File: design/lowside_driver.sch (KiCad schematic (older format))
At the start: 4 parts

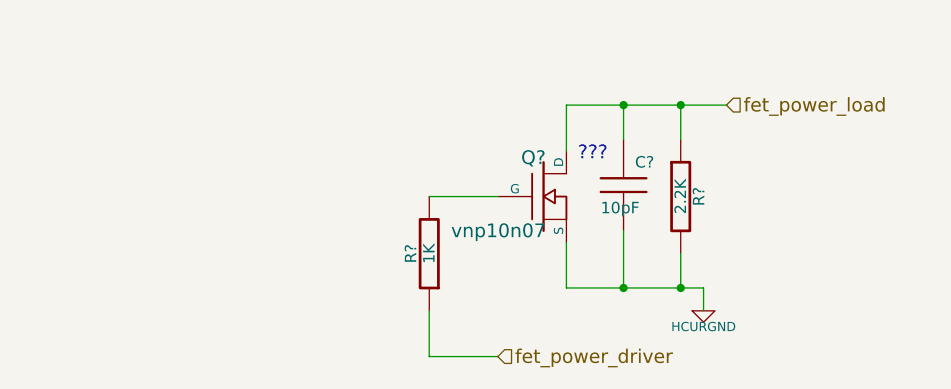
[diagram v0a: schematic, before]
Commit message: Dan's style schema in KiCAD first uploaded
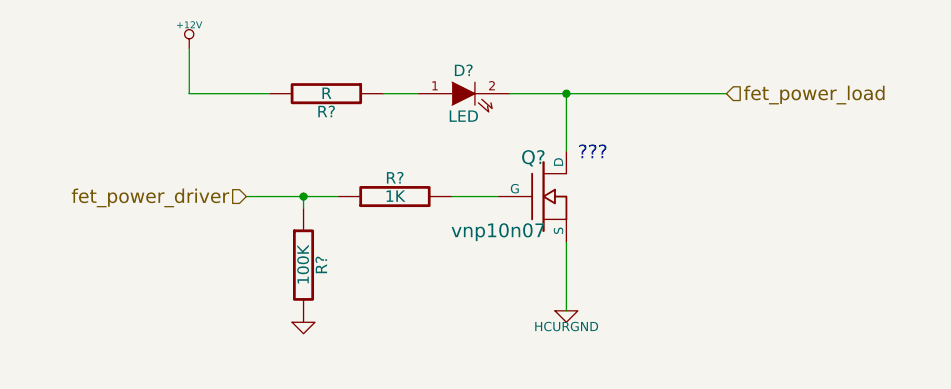
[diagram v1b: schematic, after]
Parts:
- removed C?: 10pF, symbol C
- removed R?: 2.2K, symbol R
- added D?: LED, symbol LED
- added R?: 100K, symbol R
- added R?: R, symbol R
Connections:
- net fet_power_driver: now also R?.1
- net fet_power_load: now also D?.2 (K)
- new net: D?.1 (A), R?.1
- new net +12V: R?.2
- new net GND: R?.2
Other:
- moved on the sheet: R?
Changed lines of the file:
@@
-EESchema Schematic File Version 2  date 08/10/2011 12:36:15
+EESchema Schematic File Version 2  date 10/10/2011 12:34:13
 LIBS:power
 LIBS:device
@@
 EELAYER END
 $Descr A4 11700 8267
-Sheet 14 29
+Sheet 14 20
 Title "low side driver"
-Date "8 oct 2011"
+Date "10 oct 2011"
 Rev "0.01"
 Comp "diyefi.org"
@@
 Comment4 ""
 $EndDescr
-Connection ~ 6150 4150
+Connection ~ 5650 3300
 Wire Wire Line
-	6250 4150 6250 4250
+	5650 3550 5650 3300
 Wire Wire Line
-	6250 4150 5650 4150
-Connection ~ 6150 3350
+	4850 3300 5000 3300
+Connection ~ 4500 3750
 Wire Wire Line
-	6150 3350 6150 3500
+	4500 3800 4500 3750
 Wire Wire Line
-	5900 3900 5900 4150
+	5150 3750 5350 3750
 Wire Wire Line
-	5050 3750 5350 3750
+	4650 3750 4250 3750
 Wire Wire Line
-	5650 3550 5650 3350
+	5650 4250 5650 3950
 Wire Wire Line
-	5900 3500 5900 3350
+	5400 3300 6350 3300
 Wire Wire Line
-	5650 4150 5650 3950
+	4350 3300 4000 3300
 Wire Wire Line
-	5650 3350 6350 3350
-Connection ~ 5900 3350
-Wire Wire Line
-	5050 4250 5050 4450
-Wire Wire Line
-	5050 4450 5350 4450
-Wire Wire Line
-	6150 4150 6150 4000
-Connection ~ 5900 4150
+	4000 3300 4000 3100
+$Comp
+L +12V #PWR?
+U 1 1 4E912486
+P 4000 3100
+AR Path="/4E8D66C5/4E912486" Ref="#PWR?"  Part="1"
+AR Path="/4E8D6593/4E912486" Ref="#PWR?"  Part="1"
+AR Path="/4E8D6540/4E912486" Ref="#PWR?"  Part="1"
+AR Path="/4E8D640E/4E912486" Ref="#PWR?"  Part="1"
+AR Path="/4E8D5F70/4E912486" Ref="#PWR?"  Part="1"
+F 0 "#PWR?" H 4000 3050 20  0001 C CNN
+F 1 "+12V" H 4000 3200 30  0000 C CNN
+	1    4000 3100
+	1    0    0    -1
+$EndComp
 $Comp
 L R R?
-U 1 1 4E8DCA58
-P 6150 3750
-AR Path="/4E8D5F70/4E8DCA58" Ref="R?"  Part="1"
-AR Path="/4E8D6593/4E8DCA58" Ref="R?"  Part="1"
-AR Path="/4E8D64D8/4E8DCA58" Ref="R?"  Part="1"
-AR Path="/4E8D66C5/4E8DCA58" Ref="R?"  Part="1"
-AR Path="/4E8D640E/4E8DCA58" Ref="R?"  Part="1"
-AR Path="/4E8D6540/4E8DCA58" Ref="R?"  Part="1"
-F 0 "R?" V 6230 3750 50  0000 C CNN
-F 1 "2.2K" V 6150 3750 50  0000 C CNN
-	1    6150 3750
+U 1 1 4E912449
+P 4600 3300
+AR Path="/4E8D66C5/4E912449" Ref="R?"  Part="1"
+AR Path="/4E8D6593/4E912449" Ref="R?"  Part="1"
+AR Path="/4E8D6540/4E912449" Ref="R?"  Part="1"
+AR Path="/4E8D640E/4E912449" Ref="R?"  Part="1"
+AR Path="/4E8D5F70/4E912449" Ref="R?"  Part="1"
+F 0 "R?" V 4680 3300 50  0000 C CNN
+F 1 "R" V 4600 3300 50  0000 C CNN
+	1    4600 3300
+	0    1    1    0
+$EndComp
+$Comp
+L LED D?
+U 1 1 4E912443
+P 5200 3300
+AR Path="/4E8D66C5/4E912443" Ref="D?"  Part="1"
+AR Path="/4E8D6593/4E912443" Ref="D?"  Part="1"
+AR Path="/4E8D6540/4E912443" Ref="D?"  Part="1"
+AR Path="/4E8D640E/4E912443" Ref="D?"  Part="1"
+AR Path="/4E8D5F70/4E912443" Ref="D?"  Part="1"
+F 0 "D?" H 5200 3400 50  0000 C CNN
+F 1 "LED" H 5200 3200 50  0000 C CNN
+	1    5200 3300
+	1    0    0    -1
+$EndComp
+$Comp
+L GND #PWR?
+U 1 1 4E91226E
+P 4500 4300
+AR Path="/4E8D6593/4E91226E" Ref="#PWR?"  Part="1"
+AR Path="/4E8D6540/4E91226E" Ref="#PWR?"  Part="1"
+AR Path="/4E8D66C5/4E91226E" Ref="#PWR?"  Part="1"
+AR Path="/4E8D640E/4E91226E" Ref="#PWR?"  Part="1"
+AR Path="/4E8D5F70/4E91226E" Ref="#PWR?"  Part="1"
+F 0 "#PWR?" H 4500 4300 30  0001 C CNN
+F 1 "GND" H 4500 4230 30  0001 C CNN
+	1    4500 4300
+	1    0    0    -1
+$EndComp
+$Comp
+L R R?
+U 1 1 4E91207E
+P 4500 4050
+AR Path="/4E8D6593/4E91207E" Ref="R?"  Part="1"
+AR Path="/4E8D6540/4E91207E" Ref="R?"  Part="1"
+AR Path="/4E8D66C5/4E91207E" Ref="R?"  Part="1"
+AR Path="/4E8D640E/4E91207E" Ref="R?"  Part="1"
+AR Path="/4E8D5F70/4E91207E" Ref="R?"  Part="1"
+F 0 "R?" V 4580 4050 50  0000 C CNN
+F 1 "100K" V 4500 4050 50  0000 C CNN
+	1    4500 4050
 	1    0    0    -1
 $EndComp
@@
 L HCURGND #PWR?
 U 1 1 4E8D6378
-P 6250 4250
+P 5650 4250
 AR Path="/4E8D5F70/4E8D6378" Ref="#PWR?"  Part="1"
 AR Path="/4E8D640E/4E8D6378" Ref="#PWR?"  Part="1"
@@
 AR Path="/4E8D6593/4E8D6378" Ref="#PWR?"  Part="1"
 AR Path="/4E8D6540/4E8D6378" Ref="#PWR?"  Part="1"
-F 0 "#PWR?" H 6250 4250 40  0001 C CNN
-F 1 "HCURGND" H 6250 4180 40  0000 C CNN
-	1    6250 4250
+F 0 "#PWR?" H 5650 4250 40  0001 C CNN
+F 1 "HCURGND" H 5650 4180 40  0000 C CNN
+	1    5650 4250
 	1    0    0    -1
 $EndComp
-Text HLabel 6350 3350 2    60   Input ~ 0
+Text HLabel 6350 3300 2    60   Input ~ 0
 fet_power_load
 Text Notes 5700 3600 0    60   ~ 0
 ???
-$Comp
-L C C?
-U 1 1 4E8D61E7
-P 5900 3700
-AR Path="/4E8D5F70/4E8D61E7" Ref="C?"  Part="1"
-AR Path="/4E8D640E/4E8D61E7" Ref="C?"  Part="1"
-AR Path="/4E8D64D8/4E8D61E7" Ref="C?"  Part="1"
-AR Path="/4E8D66C5/4E8D61E7" Ref="C?"  Part="1"
-AR Path="/4E8D6593/4E8D61E7" Ref="C?"  Part="1"
-AR Path="/4E8D6540/4E8D61E7" Ref="C?"  Part="1"
-F 0 "C?" H 5950 3800 50  0000 L CNN
-F 1 "10pF" H 5800 3600 50  0000 L CNN
-	1    5900 3700
-	1    0    0    -1
-$EndComp
-Text HLabel 5350 4450 2    60   Input ~ 0
+Text HLabel 4250 3750 0    60   Input ~ 0
 fet_power_driver
 $Comp
 L R R?
 U 1 1 4E8D5FDE
-P 5050 4000
+P 4900 3750
 AR Path="/4E8D5F70/4E8D5FDE" Ref="R?"  Part="1"
 AR Path="/4E8D640E/4E8D5FDE" Ref="R?"  Part="1"
@@
 AR Path="/4E8D6593/4E8D5FDE" Ref="R?"  Part="1"
 AR Path="/4E8D6540/4E8D5FDE" Ref="R?"  Part="1"
-F 0 "R?" V 5130 4000 50  0000 C CNN
-F 1 "1K" V 5050 4000 50  0000 C CNN
-	1    5050 4000
-	-1   0    0    1
+F 0 "R?" V 4980 3750 50  0000 C CNN
+F 1 "1K" V 4900 3750 50  0000 C CNN
+	1    4900 3750
+	0    -1   -1   0
 $EndComp
 $Comp
